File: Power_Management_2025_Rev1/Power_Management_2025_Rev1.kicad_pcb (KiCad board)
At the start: 2 copper layers, 213.1 x 179.3 mm, 100 parts, among them J1 RJ45_LED_Shielded, Q1 BSS138, Q2 IPB180N10S4-02, Q3 IPB180N10S4-02, Q4 IPB180N10S4-02, U1 Teensy4.1_DEV-16771, U10 LT1910, U11 LT1910, U12 PKE3316ZPI, U13 PKE3316ZPI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

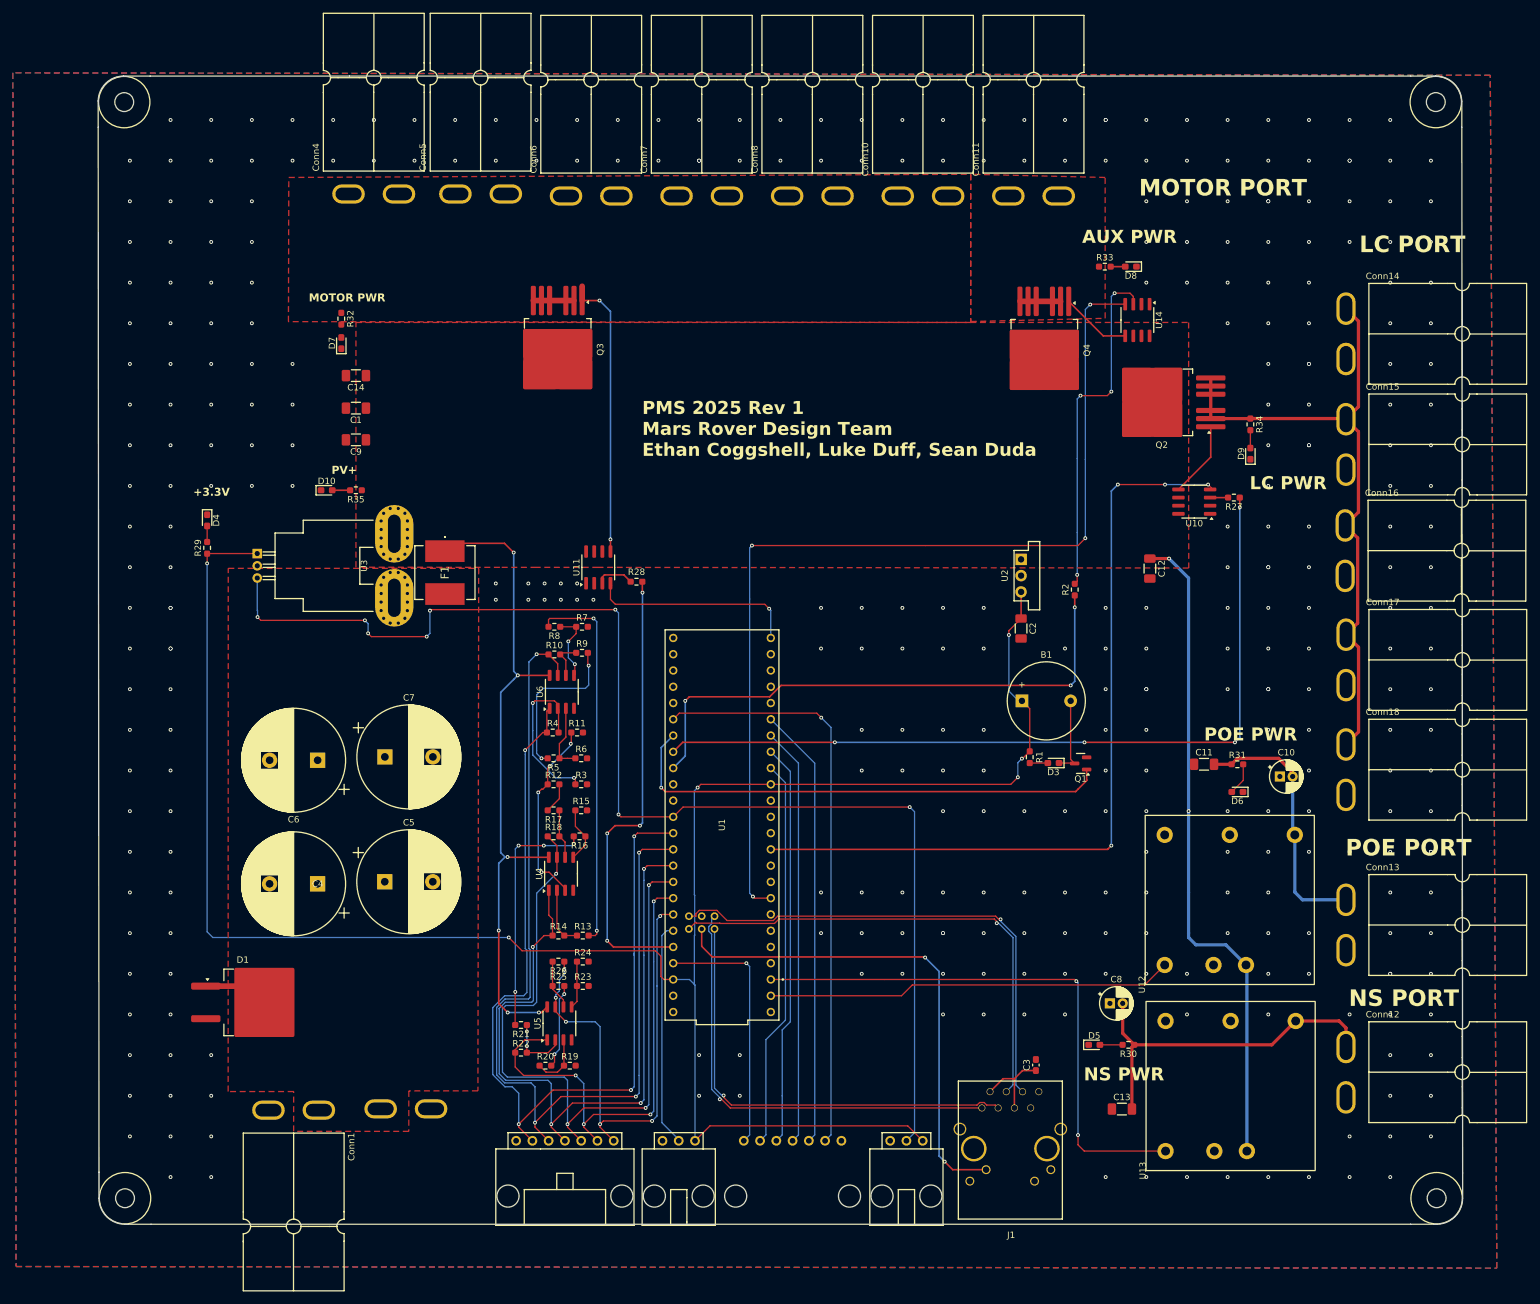
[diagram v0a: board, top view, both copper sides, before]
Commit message: Worked on corrections
Retraced opamp circuit, fixed diff pair, moved capacitors to be closer to what they filter, increased size of silkscreens, fixed inputs and outputs in relation to opamps and teensie
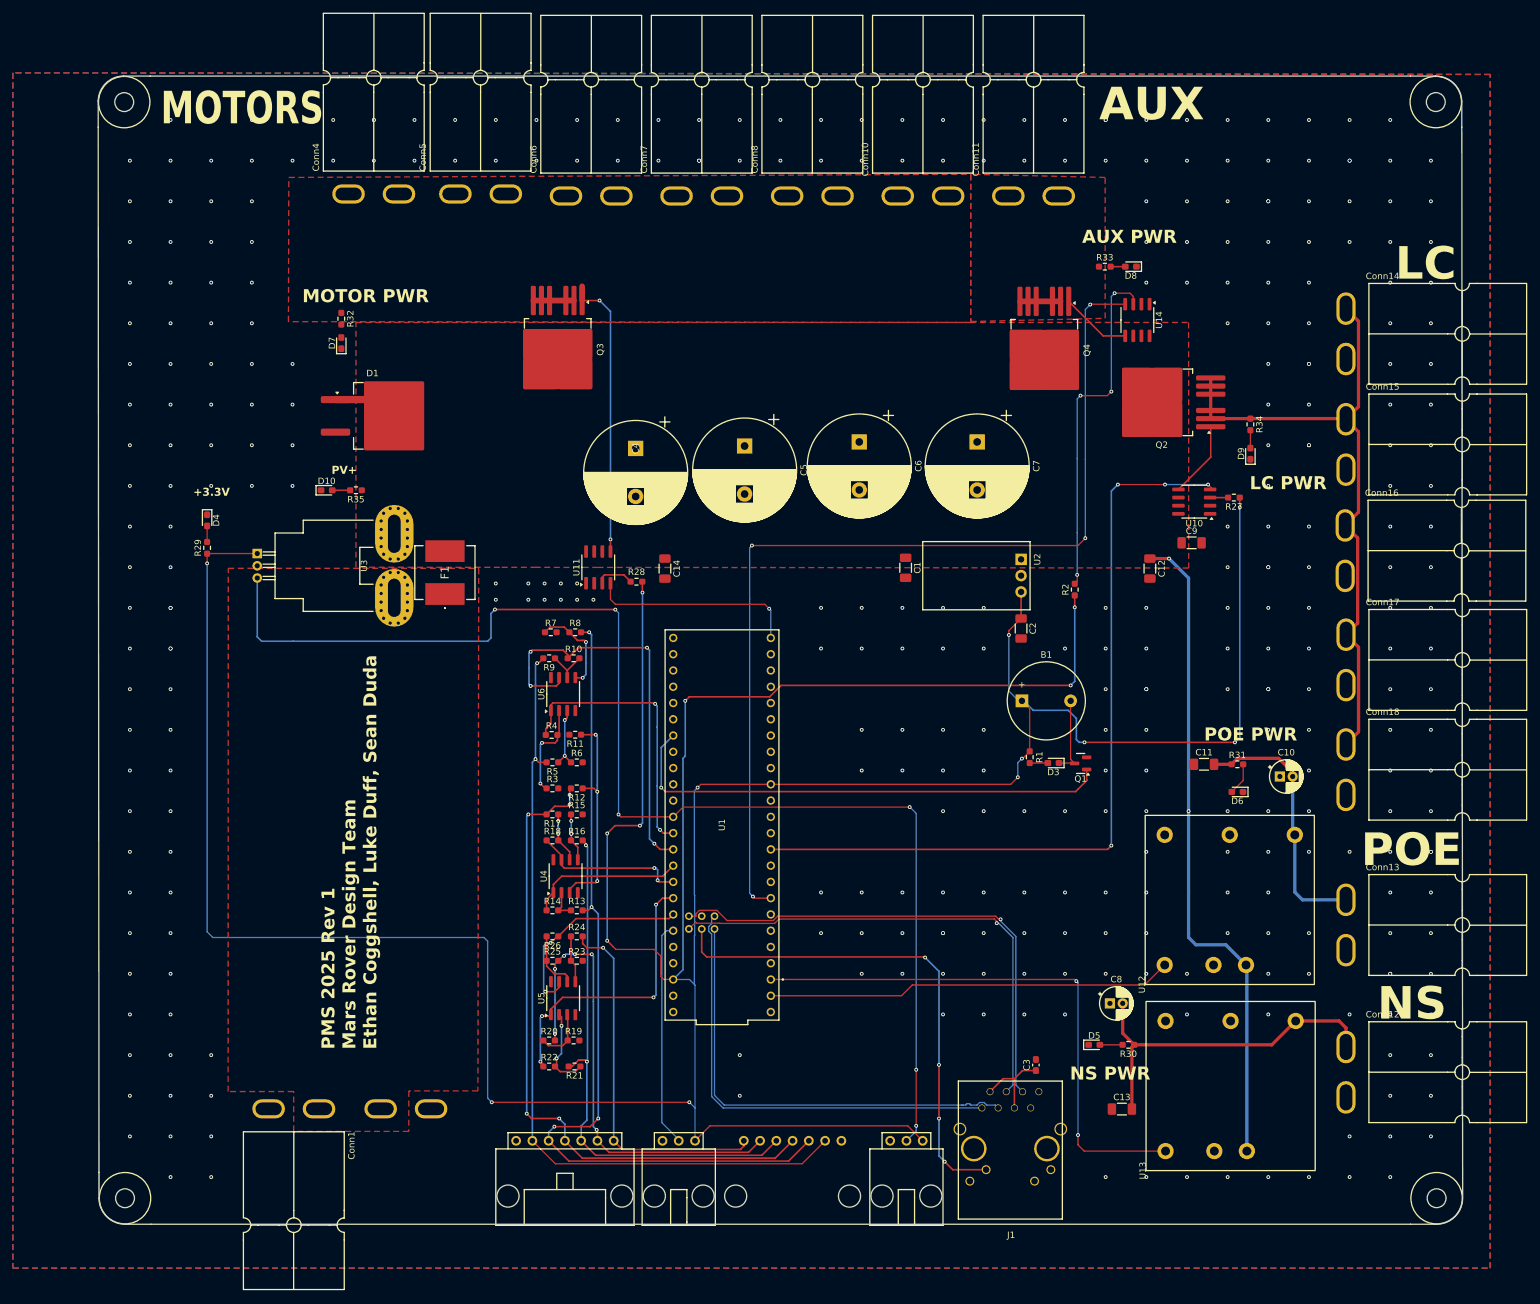
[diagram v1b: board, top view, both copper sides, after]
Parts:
- U2: footprint Converter_DCDC:Converter_DCDC_Murata_OKI-78SR_Vertical -> Converter_DCDC:Converter_DCDC_Murata_OKI-78SR_Horizontal
- moved C9 131.5 mm to (197.6, 85.1), turned to 0 degrees
- moved C7 104.8 mm to (164.1, 69.3), turned to -90 degrees
- moved C6 98.1 mm to (145.7, 69.3), turned to -90 degrees
- moved D1 93.8 mm to (71.5, 65.3)
- moved C1 89.4 mm to (152.9, 89.0), turned to -90 degrees
- moved C5 88.3 mm to (127.8, 70.0), turned to -90 degrees
- moved C4 84.2 mm to (110.7, 70.4), turned to -90 degrees
- moved C14 56.9 mm to (115.3, 89.1), turned to -90 degrees
- moved R21 10.6 mm to (101.2, 166.9)
- moved R9 5.20 mm to (97.2, 103.1), turned to 180 degrees
- moved R7 4.95 mm to (97.5, 99.1)
- moved R22 4.90 mm to (97.2, 166.9)
- moved R3 4.54 mm to (97.7, 123.4)
- moved R13 4.05 mm to (101.6, 142.5)
- moved R14 4.05 mm to (97.7, 142.5)
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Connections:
- C4 pad 1: IP+ -> IP-
- C5 pad 1: IP+ -> IP-
- C6 pad 1: IP+ -> IP-
- C7 pad 1: IP+ -> IP-
- Conn2 pad 1: CELL_SENSE_6 -> CELL6
- Conn2 pad 2: CELL_SENSE_5 -> CELL5
- Conn2 pad 3: CELL_SENSE_4 -> CELL4
- Conn2 pad 4: CELL_SENSE_3 -> CELL3
- Conn2 pad 5: CELL_SENSE_2 -> CELL2
- Conn2 pad 6: CELL_SENSE_1 -> CELL1
- Conn20 pad 1: CELL_SENSE2_6 -> CELL6
- Conn20 pad 2: CELL_SENSE2_5 -> CELL5
- Conn20 pad 3: CELL_SENSE2_4 -> CELL4
- Conn20 pad 4: CELL_SENSE2_3 -> CELL3
- Conn20 pad 5: CELL_SENSE2_2 -> CELL2
- Conn20 pad 6: CELL_SENSE2_1 -> CELL1
- D1 pad 1: IP+ -> IP-
- F1 pad 1: IP- -> IP+
- F1 pad 2: IP+ -> IP-
- R2 pad 1: FF_AUX -> +3.3V
- R27 pad 1: FF_LC -> +3.3V
- R28 pad 1: FF_MOTOR -> +3.3V
- U1 pad 22: FF_MOTOR -> unconnected-(U1-A8-Pad22)
- U1 pad 23: CELL_SENSE2_6 -> unconnected-(U1-A9-Pad23)
- U1 pad 24: CELL_SENSE2_5 -> unconnected-(U1-A10-Pad24)
- U1 pad 25: CELL_SENSE2_4 -> unconnected-(U1-A11-Pad25)
- U1 pad 26: CELL_SENSE2_3 -> unconnected-(U1-A12-Pad26)
- U1 pad 27: CELL_SENSE2_2 -> unconnected-(U1-A13-Pad27)
- U1 pad 38: CELL_SENSE2_1 -> unconnected-(U1-A14-Pad38)
- U1 pad 40: FF_LC -> unconnected-(U1-A16-Pad40)
- U1 pad 41: FF_AUX -> unconnected-(U1-A17-Pad41)
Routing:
- net +3.3V: track 324.2 -> 620.0 mm, vias 6 -> 17
- net FF_LC: track 126.9 -> 0.00 mm, vias 4 -> 0
- net CELL1: track 25.0 -> 126.8 mm
- net CELL_SENSE_1: track 143.2 -> 43.8 mm, vias 4 -> 2
- net CELL3: track 4.82 -> 103.6 mm, vias 0 -> 5
- net CELL_SENSE_4: track 116.8 -> 24.3 mm, vias 4 -> 2
- net CELL_SENSE2_1: track 90.9 -> 0.00 mm, vias 1 -> 0
- net IP-: track 206.1 -> 116.5 mm, vias 8 -> 2
- net CELL_SENSE_2: track 153.7 -> 65.3 mm
- net FF_AUX: track 86.8 -> 0.00 mm, vias 3 -> 0
- net CELL_SENSE_3: track 111.1 -> 24.4 mm, vias 4 -> 0
- net CELL2: track 59.1 -> 132.6 mm, vias 2 -> 4
- net FF_MOTOR: track 71.4 -> 0.00 mm, vias 4 -> 0
- net CELL_SENSE2_2: track 69.1 -> 0.00 mm
- net CELL_SENSE2_3: track 65.5 -> 0.00 mm
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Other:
- board text added: "AUX"
- board text added: "LC"
- board text added: "MOTORS"
- board text added: "NS"
- board text added: "POE"
- board text removed: "LC PORT"
- board text removed: "MOTOR PORT"
- board text removed: "NS PORT"
- board text removed: "POE PORT"

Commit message: Changed Silkscreen
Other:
- board text added: "PMS 2025 Rev 1 Mars Rover Design Team Ethan Coggeshell, Luke Duff, Sean Duda"
- board text removed: "PMS 2025 Rev 1 Mars Rover Design Team Ethan Coggshell, Luke Duff, Sean Duda"
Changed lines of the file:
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@@
 		(tags "resistor handsolder")
 		(property "Reference" "R16"
-			(at 0 -1.43 360)
+			(at 0 -1.43 0)
 			(layer "F.SilkS")
 			(effects
@@
 		)
 		(property "Value" "47k"
-			(at 0 1.43 360)
+			(at 0 1.43 0)
 			(layer "F.Fab")
 			(effects
@@
 		)
 		(fp_text user "${REFERENCE}"
-			(at 0.1505 0 360)
+			(at 0.1505 0 0)
 			(layer "F.Fab")
 			(effects
@@
 		(tags "capacitor handsolder")
 		(property "Reference" "C9"
-			(at 0 -1.85 360)
+			(at 0 -1.85 0)
 			(layer "F.SilkS")
 			(effects
@@
 		)
 		(property "Value" "10uF"
-			(at 0 1.85 360)
+			(at 0 1.85 0)
 			(layer "F.Fab")
 			(effects
@@
 		)
 		(fp_text user "${REFERENCE}"
-			(at 0 0 360)
+			(at 0 0 0)
 			(layer "F.Fab")
 			(effects
@@
 		(tags "resistor handsolder")
 		(property "Reference" "R9"
-			(at 0 -1.43 360)
+			(at 0 -1.43 0)
 			(layer "F.SilkS")
 			(effects
@@
 		)
 		(property "Value" "47k"
-			(at 0 1.43 360)
+			(at 0 1.43 0)
 			(layer "F.Fab")
 			(effects
@@
 		)
 		(fp_text user "${REFERENCE}"
-			(at 0 0 360)
+			(at 0 0 0)
 			(layer "F.Fab")
 			(effects
@@
 		(tags "resistor handsolder")
 		(property "Reference" "R8"
-			(at 0 -1.43 360)
+			(at 0 -1.43 0)
 			(layer "F.SilkS")
 			(effects
@@
 		)
 		(property "Value" "47k"
-			(at 0 1.43 360)
+			(at 0 1.43 0)
 			(layer "F.Fab")
 			(effects
@@
 		)
 		(fp_text user "${REFERENCE}"
-			(at 0 0 360)
+			(at 0 0 0)
 			(layer "F.Fab")
 			(effects
@@
 		(tags "D2PAK DDPAK TO-263 D2PAK-3 TO-263-3 SOT-404 diode")
 		(property "Reference" "D1"
-			(at -1.875 -6.65 360)
+			(at -1.875 -6.65 0)
 			(layer "F.SilkS")
 			(effects
@@
 		)
 		(property "Value" "D_Schottky"
-			(at -1.875 6.65 360)
+			(at -1.875 6.65 0)
 			(layer "F.Fab")
 			(effects
@@
 		)
 		(fp_text user "${REFERENCE}"
-			(at -1.875 0 360)
+			(at -1.875 0 0)
 			(layer "F.Fab")
 			(effects
@@
 		(tags "resistor handsolder")
 		(property "Reference" "R11"
-			(at 0 -1.43 360)
+			(at 0 -1.43 0)
 			(layer "F.SilkS")
 			(effects
@@
 		)
 		(property "Value" "39k"
-			(at 0 1.43 360)
+			(at 0 1.43 0)
 			(layer "F.Fab")
 			(effects
@@
 		)
 		(fp_text user "${REFERENCE}"
-			(at 0 0 360)
+			(at 0 0 0)
 			(layer "F.Fab")
 			(effects
@@
 		(tags "resistor handsolder")
 		(property "Reference" "R12"
-			(at 0 -1.43 360)
+			(at 0 -1.43 0)
 			(layer "F.SilkS")
 			(effects
@@
 		)
 		(property "Value" "47k"
-			(at -0.3575 1.524 360)
+			(at -0.3575 1.524 0)
 			(layer "F.Fab")
 			(effects
@@
 		)
 		(fp_text user "${REFERENCE}"
-			(at 0 0 360)
+			(at 0 0 0)
 			(layer "F.Fab")
 			(effects
@@
 		)
 	)
-	(gr_text "PMS 2025 Rev 1\nMars Rover Design Team\nEthan Coggshell, Luke Duff, Sean Duda"
+	(gr_text "PMS 2025 Rev 1\nMars Rover Design Team\nEthan Coggeshell, Luke Duff, Sean Duda"
 		(at 70.485 164.211 90)
 		(layer "F.SilkS")

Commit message: We changed the planes
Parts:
- Conn20: moved to F.Cu
- moved C7 116.3 mm to (62.0, 125.0), turned to 0 degrees
- moved C6 86.6 mm to (79.3, 125.0), turned to 0 degrees
- moved D1 71.2 mm to (51.4, 133.6)
- moved C5 61.7 mm to (79.3, 108.2), turned to 0 degrees
- moved C4 61.7 mm to (62.0, 108.2), turned to 0 degrees
- moved F1 49.8 mm to (81.3, 139.5)
- moved Conn9 22.7 mm to (142.7, 178.4)
- moved Conn20 2.42 mm to (130.0, 178.4), turned to 180 degrees
- moved U3 0.28 mm to (51.7, 86.5)
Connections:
- C4 pad 1: IP- -> PV-
- C5 pad 1: IP- -> PV-
- C6 pad 1: IP- -> PV-
- C7 pad 1: IP- -> PV-
- Conn1 pad 4: IP+ -> PV+
- Conn19 pad 4: IP+ -> PV+
- D1 pad 1: IP- -> PV-
- F1 pad 1: IP+ -> PV+
- F1 pad 2: IP- -> PV-
- U3 pad 4: IP+ -> PV-
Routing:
- net IP-: track 116.5 -> 187.8 mm, vias 2 -> 5
- net TEMP_SENSE: track 35.2 -> 57.9 mm, vias 0 -> 1
- net CELL1: track 126.8 -> 108.4 mm, vias 2 -> 3
- net CELL3: track 103.6 -> 93.0 mm, vias 5 -> 6
- net PV-: track 0.00 -> 10.2 mm
- net CELL2: track 132.6 -> 123.0 mm, vias 4 -> 5
- net CELL4: track 84.1 -> 78.5 mm, vias 2 -> 3
- net CELL6: track 57.4 -> 59.3 mm
- net +3.3V: track 620.0 -> 618.5 mm, vias 17 -> 18
- net CELL5: track 74.7 -> 73.3 mm, vias 6 -> 7
- added copper zone on F.Cu, net PV+
- added copper zone on F.Cu, net PV-
- removed copper zone on F.Cu, net IP+
